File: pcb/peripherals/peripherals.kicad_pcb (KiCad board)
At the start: 2 copper layers, 31 parts, among them J1 JST XH, J10 JST XH, J11 JST XH, J2 JST XH, J3 Pin header, J4 Pin header, J5 JST XH, J6 JST XH, J7 JST XH, J8 JST XH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

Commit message: Route more tracks.
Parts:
- D1, D2: footprint Diode_THT:D_A-405_P10.16mm_Horizontal -> Diode_THT:D_A-405_P5.08mm_Vertical_KathodeUp
- moved J2 153.5 mm to (5.71, 57.1), turned to 90 degrees
- moved J8 151.5 mm to (26.0, 96.5), turned to 270 degrees
- moved J5 144.9 mm to (37.5, 96.5), turned to 270 degrees
- moved J1 115.0 mm to (14.0, 57.1), turned to 90 degrees
- moved REF** 110.5 mm to (128.3, 99.1)
- moved REF** 90.8 mm to (5.71, 101.6)
- moved J7 76.8 mm to (48.3, 96.5), turned to 270 degrees
- moved R1 69.5 mm to (44.5, 88.9)
- moved R3 69.3 mm to (44.5, 81.9)
- moved U2 68.9 mm to (97.8, 52.7), turned to 180 degrees
- moved REF** 64.1 mm to (127.0, 35.6)
- moved R5 63.5 mm to (50.2, 75.6)
- moved J11 57.8 mm to (125.7, 45.1), turned to 270 degrees
- moved J9 57.5 mm to (125.7, 83.8), turned to 270 degrees
- moved J6 52.8 mm to (15.2, 96.5), turned to 270 degrees
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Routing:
- net GND: track 0.00 -> 244.6 mm, vias 0 -> 2
- net +5V: track 0.00 -> 92.4 mm
- net SDA: track 0.00 -> 67.3 mm, vias 0 -> 2
- net +5VP: track 0.00 -> 59.4 mm, vias 0 -> 2
- net SCL: track 0.00 -> 57.2 mm
- net Net-(A1-Pad19): track 0.00 -> 51.6 mm, vias 0 -> 2
- net Net-(J3-Pad2): track 0.00 -> 40.8 mm, vias 0 -> 2
- net Net-(J4-Pad2): track 0.00 -> 36.2 mm, vias 0 -> 2
- net Net-(J1-Pad2): track 0.00 -> 8.26 mm

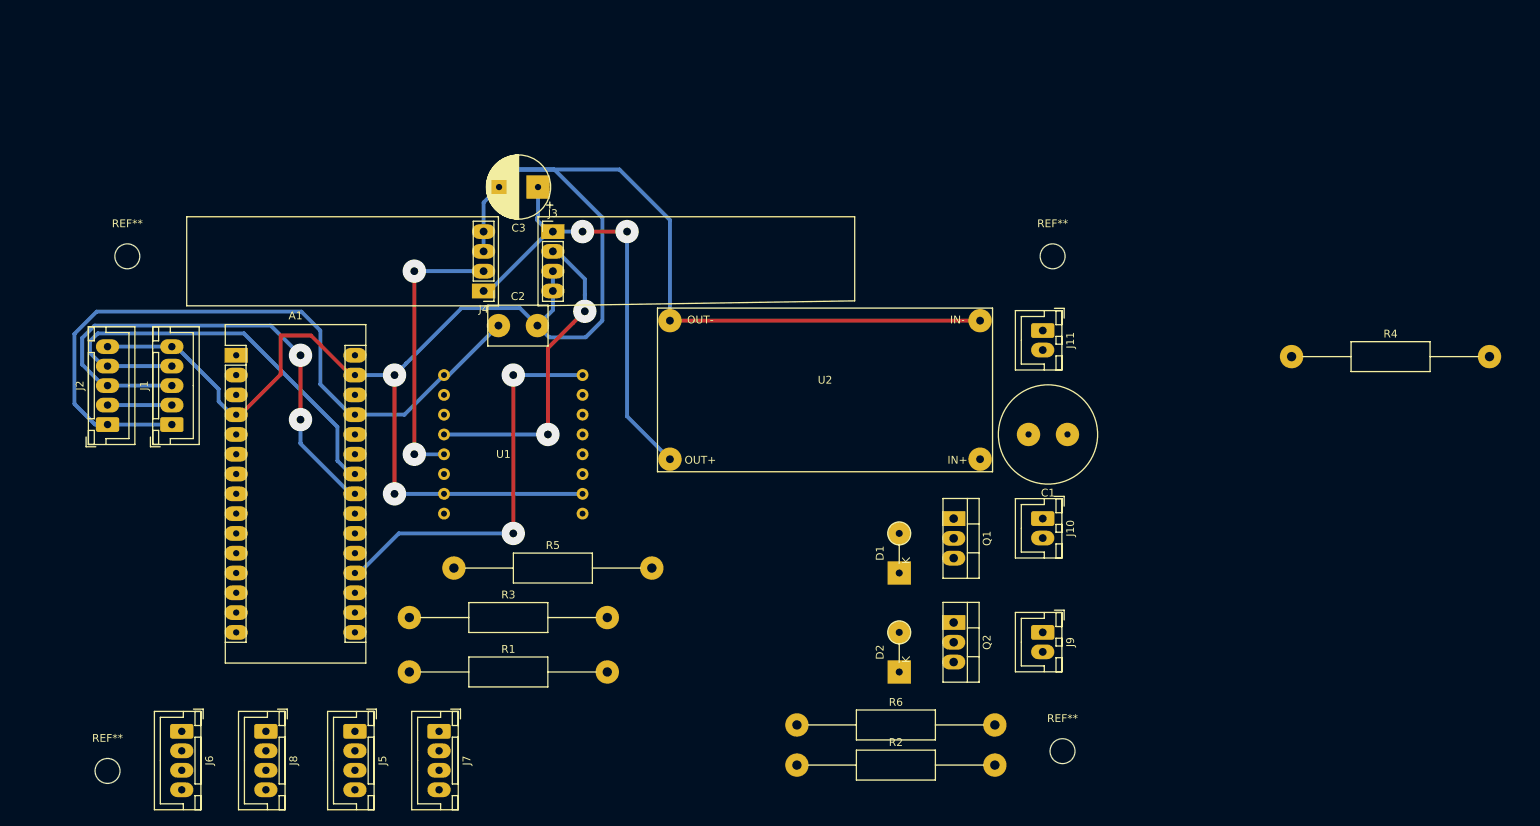
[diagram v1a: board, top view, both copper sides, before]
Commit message: Complete routing.
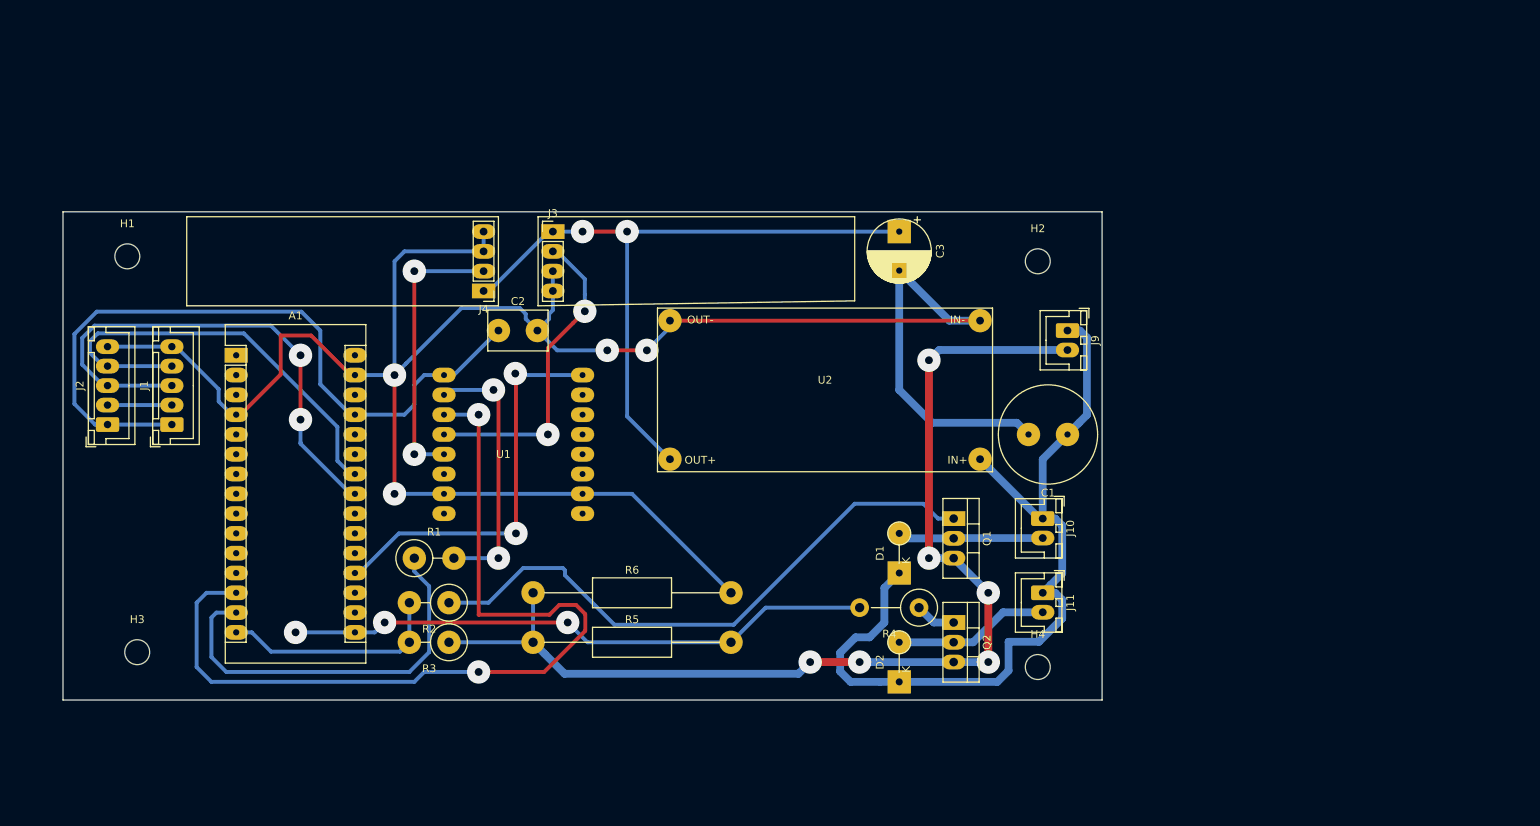
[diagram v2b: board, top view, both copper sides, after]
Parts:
- removed J5, J6, J7, J8: JST XH, Connector_JST:JST_XH_B04B-XH-A_1x04_P2.50mm_Vertical
- removed REF** (x4): MountingHole_3.2mm_M3, MountingHole:MountingHole_3.2mm_M3
- added H1: MountingHole, MountingHole:MountingHole_3.2mm_M3, F.Cu at (8.26, 35.6)
- added H2: MountingHole, MountingHole:MountingHole_3.2mm_M3, F.Cu at (125.1, 36.2)
- added H3: MountingHole, MountingHole:MountingHole_3.2mm_M3, F.Cu at (9.53, 86.4)
- added H4: MountingHole, MountingHole:MountingHole_3.2mm_M3, F.Cu at (125.1, 88.3)
- R1, R2, R3: footprint Resistor_THT:R_Axial_DIN0411_L9.9mm_D3.6mm_P25.40mm_Horizontal -> Resistor_THT:R_Axial_DIN0414_L11.9mm_D4.5mm_P5.08mm_Vertical
- R4: footprint Resistor_THT:R_Axial_DIN0411_L9.9mm_D3.6mm_P25.40mm_Horizontal -> Resistor_THT:R_Axial_DIN0414_L11.9mm_D4.5mm_P7.62mm_Vertical
- moved R4 57.7 mm to (109.9, 80.6), turned to 180 degrees
- moved R2 49.3 mm to (49.5, 80.0), turned to 180 degrees
- moved C3 46.7 mm to (107.3, 32.4), turned to 270 degrees
- moved J9 38.9 mm to (128.9, 45.1)
- moved R6 37.9 mm to (60.3, 78.7)
- moved J11 33.7 mm to (125.7, 78.7)
- moved R1 14.6 mm to (45.1, 74.3)
- moved R5 13.9 mm to (60.3, 85.1)
- moved R3 5.99 mm to (49.5, 85.1), turned to 180 degrees
- moved D2 1.27 mm to (107.3, 90.2)
- moved C2 0.63 mm to (55.9, 45.1)
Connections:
- A1 pad 10: IO6 -> Net-(A1-Pad10)
- A1 pad 11: IO7 -> Net-(A1-Pad11)
- A1 pad 12: IO8 -> Net-(A1-Pad12)
- A1 pad 5: IO1 -> Net-(A1-Pad5)
- A1 pad 6: IO2 -> Net-(A1-Pad6)
- A1 pad 7: IO3 -> Net-(A1-Pad7)
- A1 pad 8: IO4 -> Net-(A1-Pad8)
- A1 pad 9: IO5 -> Net-(A1-Pad9)
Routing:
- net GNDPWR: track 0.00 -> 139.9 mm, vias 0 -> 6
- net Net-(A1-Pad13): track 0.00 -> 114.2 mm, vias 0 -> 2
- net +24V: track 0.00 -> 108.9 mm
- net Net-(Q1-Pad1): track 0.00 -> 77.2 mm
- net PWM2: track 0.00 -> 75.8 mm, vias 0 -> 3
- net Net-(A1-Pad14): track 0.00 -> 51.2 mm
- net GND: track 244.6 -> 282.5 mm, vias 2 -> 4
- net Net-(R1-Pad2): track 0.00 -> 34.2 mm, vias 0 -> 2
- net PWM1: track 0.00 -> 28.8 mm
- net +5VP: track 59.4 -> 88.0 mm
- net Net-(D2-Pad2): track 0.00 -> 20.0 mm
- net Net-(D1-Pad2): track 0.00 -> 18.7 mm
- net Net-(Q2-Pad1): track 0.00 -> 5.23 mm
- net +5V: track 92.4 -> 94.3 mm
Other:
- board outline added: 133.3 x 62.7 mm

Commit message: Update.
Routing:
- net PWM2: track 75.8 -> 68.2 mm, vias 3 -> 2
- net +5VP: vias 2 -> 0
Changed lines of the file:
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@@
     (thickness 1.6)
     (drawings 12)
-    (tracks 250)
+    (tracks 246)
     (zones 0)
     (modules 27)
@@
   )
   (setup
-    (last_trace_width 0.5)
+    (last_trace_width 1)
     (user_trace_width 0.5)
     (trace_clearance 0.5)
@@
       (effects (font (size 1 1) (thickness 0.15)))
     )
-    (pad 1 thru_hole circle (at 0 0 180) (size 2.4 2.4) (drill 1.2) (layers *.Cu *.Mask)
+    (pad 1 thru_hole circle (at 0 0 180) (size 3 3) (drill 1.2) (layers *.Cu *.Mask)
       (net 31 "Net-(Q2-Pad1)"))
-    (pad 2 thru_hole oval (at 7.62 0 180) (size 2.4 2.4) (drill 1.2) (layers *.Cu *.Mask)
+    (pad 2 thru_hole oval (at 7.62 0 180) (size 3 3) (drill 1.2) (layers *.Cu *.Mask)
       (net 21 PWM2))
     (model ${KISYS3DMOD}/Resistor_THT.3dshapes/R_Axial_DIN0414_L11.9mm_D4.5mm_P7.62mm_Vertical.wrl
@@
   (segment (start 26.694999 86.289999) (end 24.225 83.82) (width 0.5) (layer B.Cu) (net 20))
   (segment (start 44.45 85.09) (end 43.250001 86.289999) (width 0.5) (layer B.Cu) (net 20))
-  (via (at 29.845 83.82) (size 3) (drill 1) (layers F.Cu B.Cu) (net 21))
-  (segment (start 37.465 83.82) (end 29.845 83.82) (width 0.5) (layer B.Cu) (net 21))
   (segment (start 90.17 80.645) (end 85.725 85.09) (width 0.5) (layer B.Cu) (net 21))
   (via (at 41.275 82.55) (size 3) (drill 1) (layers F.Cu B.Cu) (net 21))
@@
   (segment (start 54.695 40.005) (end 62.315 32.385) (width 0.5) (layer B.Cu) (net 26))
   (segment (start 53.975 40.005) (end 54.695 40.005) (width 0.5) (layer B.Cu) (net 26))
-  (via (at 66.675 32.385) (size 3) (drill 1) (layers F.Cu B.Cu) (net 26))
   (segment (start 62.865 32.385) (end 66.675 32.385) (width 0.5) (layer B.Cu) (net 26))
-  (via (at 72.39 32.385) (size 3) (drill 1) (layers F.Cu B.Cu) (net 26))
-  (segment (start 66.675 32.385) (end 72.39 32.385) (width 0.5) (layer F.Cu) (net 26))
   (segment (start 72.39 56.095) (end 77.89 61.595) (width 0.5) (layer B.Cu) (net 26))
   (segment (start 72.39 32.385) (end 72.39 56.095) (width 0.5) (layer B.Cu) (net 26))
   (segment (start 107.315 32.385) (end 72.39 32.385) (width 0.5) (layer B.Cu) (net 26))
+  (segment (start 66.675 32.385) (end 72.39 32.385) (width 0.5) (layer B.Cu) (net 26))
   (via (at 62.23 58.42) (size 3) (drill 1) (layers F.Cu B.Cu) (net 27))
   (segment (start 48.895 58.42) (end 62.23 58.42) (width 0.5) (layer B.Cu) (net 27))

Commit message: SMD version.
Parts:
- removed J10, J11: JST XH, Connector_JST:JST_XH_B02B-XH-A_1x02_P2.50mm_Vertical
- removed J4: Pin header, Connector_PinHeader_2.54mm:PinHeader_1x04_P2.54mm_Vertical
- removed U2: buck-converter, Peripherals:buck-converter
- added C4: 1u, Capacitor_SMD:C_0805_2012Metric, F.Cu at (25.4, 64.1)
- added C5: 1u, Capacitor_SMD:C_0805_2012Metric, F.Cu at (34.9, 64.1)
- added C6: 1u, Capacitor_SMD:C_0805_2012Metric, F.Cu at (64.8, 76.2)
- added C7: 1u, Capacitor_SMD:C_0805_2012Metric, F.Cu at (74.7, 76.2)
- added C9: 1u, Capacitor_SMD:C_0805_2012Metric, F.Cu at (62.9, 48.3)
- added D3: SS34, Diode_SMD:D_SMB, F.Cu at (69.8, 81.9)
- added D4: SS34, Diode_SMD:D_SMB, F.Cu at (79.4, 81.9)
- added J5: JST XH, Connector_JST:JST_XH_B02B-XH-A_1x02_P2.50mm_Vertical, F.Cu at (26.0, 87.6)
- added J6: JST XH, Connector_JST:JST_XH_B02B-XH-A_1x02_P2.50mm_Vertical, F.Cu at (35.6, 87.6)
- added J7: JST XH, Connector_JST:JST_XH_B02B-XH-A_1x02_P2.50mm_Vertical, F.Cu at (68.6, 87.6)
- added J8: JST XH, Connector_JST:JST_XH_B02B-XH-A_1x02_P2.50mm_Vertical, F.Cu at (78.1, 87.6)
- added Q3: FDD8447L, Package_TO_SOT_SMD:TO-252-2, F.Cu at (69.8, 73.7)
- added Q4: FDD8447L, Package_TO_SOT_SMD:TO-252-2, F.Cu at (79.4, 73.7)
- added R10: 47k, Resistor_SMD:R_0603_1608Metric, F.Cu at (77.5, 67.3)
- added R7: 1k, Resistor_SMD:R_0603_1608Metric, F.Cu at (71.8, 67.3)
- added R8: 47k, Resistor_SMD:R_0603_1608Metric, F.Cu at (67.9, 67.3)
- added R9: 1k, Resistor_SMD:R_0603_1608Metric, F.Cu at (81.3, 67.3)
- C1: footprint Capacitor_THT:C_Radial_D12.5mm_H20.0mm_P5.00mm -> Capacitor_SMD:CP_Elec_10x10
- C2: value 100n -> 1u; footprint Capacitor_THT:C_Disc_D7.5mm_W5.0mm_P5.00mm -> Capacitor_SMD:C_0603_1608Metric
- C3: footprint Capacitor_THT:CP_Radial_D8.0mm_P5.00mm -> Capacitor_SMD:CP_Elec_10x10
- D1, D2: value 1N4001 -> SS34; footprint Diode_THT:D_A-405_P5.08mm_Vertical_KathodeUp -> Diode_SMD:D_SMB
- J3: value Pin header -> Conn_01x03; footprint Connector_PinHeader_2.54mm:PinHeader_1x04_P2.54mm_Vertical -> Connector_JST:JST_XH_B03B-XH-A_1x03_P2.50mm_Vertical
- Q1, Q2: value IRFZ44N -> FDD8447L; footprint Package_TO_SOT_THT:TO-220-3_Vertical -> Package_TO_SOT_SMD:TO-252-2
- R1, R2, R3: footprint Resistor_THT:R_Axial_DIN0414_L11.9mm_D4.5mm_P5.08mm_Vertical -> Resistor_SMD:R_0603_1608Metric
- R4: footprint Resistor_THT:R_Axial_DIN0414_L11.9mm_D4.5mm_P7.62mm_Vertical -> Resistor_SMD:R_0603_1608Metric
- R5, R6: footprint Resistor_THT:R_Axial_DIN0411_L9.9mm_D3.6mm_P25.40mm_Horizontal -> Resistor_SMD:R_0603_1608Metric
- moved H4 119.6 mm to (19.7, 31.8)
- moved H2 117.3 mm to (19.7, 87.6)
- moved J9 108.8 mm to (20.3, 51.4)
- moved C1 99.2 mm to (29.8, 52.7), turned to 0 degrees
- moved H3 96.3 mm to (88.9, 31.8)
- moved H1 96.0 mm to (88.9, 87.6)
- moved Q1 87.1 mm to (27.3, 73.7)
- moved D1 80.2 mm to (27.3, 81.9), turned to 0 degrees
- moved Q2 78.0 mm to (36.8, 73.7)
- moved R4 72.4 mm to (38.7, 67.3)
- moved D2 71.0 mm to (36.8, 81.9), turned to 0 degrees
- moved C3 61.0 mm to (46.4, 33.7), turned to 0 degrees
- moved R1 34.4 mm to (66.0, 47.0)
- moved R6 34.4 mm to (39.4, 51.4)
- moved R5 31.0 mm to (34.9, 67.3)
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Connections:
- A1 pad 12: Net-(A1-Pad12) -> PWM4
- A1 pad 15: PWM1 -> Net-(A1-Pad15)
- A1 pad 16: PWM2 -> Net-(A1-Pad16)
- A1 pad 21: Net-(A1-Pad21) -> DFTX
- A1 pad 22: Net-(A1-Pad22) -> DFRX
- A1 pad 6: Net-(A1-Pad6) -> PWM1
- A1 pad 8: Net-(A1-Pad8) -> PWM2
- A1 pad 9: Net-(A1-Pad9) -> PWM3
- C1 pad 2: GND -> GNDPWR
- C3 pad 1: +5VP -> +5V
- J3 pad 1: +5VP -> Net-(J3-Pad1)
- J3 pad 2: Net-(J3-Pad2) -> GND
- J3 pad 3: GND -> Net-(J3-Pad3)
- R1 pad 1: Net-(A1-Pad14) -> DFRX
- U1 pad 3: Net-(A1-Pad13) -> DFTX
- U1 pad 4: Net-(J3-Pad2) -> Net-(J3-Pad3)
- U1 pad 5: Net-(J4-Pad2) -> Net-(J3-Pad1)
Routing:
- net GND: track 282.5 -> 147.1 mm, vias 4 -> 0
- net Net-(A1-Pad13): track 114.2 -> 0.00 mm, vias 2 -> 0
- net +5VP: track 88.0 -> 0.00 mm
- net Net-(Q1-Pad1): track 77.2 -> 2.32 mm
- net PWM4: track 0.00 -> 59.5 mm, vias 0 -> 1
- net PWM2: track 68.2 -> 11.9 mm, vias 2 -> 0
- net GNDPWR: track 139.9 -> 195.9 mm, vias 6 -> 0
- net Net-(A1-Pad14): track 51.2 -> 0.00 mm
- net PWM3: track 0.00 -> 47.1 mm, vias 0 -> 1
- net +24V: track 108.9 -> 152.3 mm
- net Net-(J3-Pad2): track 40.8 -> 0.00 mm, vias 2 -> 0
- net Net-(J4-Pad2): track 36.2 -> 0.00 mm, vias 2 -> 0
- net Net-(R1-Pad2): track 34.2 -> 4.29 mm, vias 2 -> 0
- net DFTX: track 0.00 -> 21.2 mm
- net Net-(J3-Pad1): track 0.00 -> 20.6 mm
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- added copper zone on F.Cu, net GND
- added copper zone on F.Cu, net GNDPWR
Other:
- board size 133.3 x 62.7 mm -> 77 x 64.5 mm
- board text added: "+"
- board text added: "24V"
- board text added: "AUDIO"
- board text added: "I2C"

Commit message: Work on layout.
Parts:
- removed the C2 at (81.9, 40.0)
- removed C7: 1u, Capacitor_SMD:C_0805_2012Metric
- removed the J3 at (71.8, 35.6)
- removed R10: 47k, Resistor_SMD:R_0603_1608Metric
- removed R9: 1k, Resistor_SMD:R_0603_1608Metric
- removed the U1 at (78.7, 44.5)
- added C4: 1u, Capacitor_SMD:C_0805_2012Metric, F.Cu at (14.0, 63.2)
- added J10: Conn_01x04, Connector_JST:JST_XH_B04B-XH-A_1x04_P2.50mm_Vertical, F.Cu at (38.3, 62.6)
- added J4: Conn_01x08, Connector_JST:JST_XH_B08B-XH-A_1x08_P2.50mm_Vertical, F.Cu at (39.1, 69.2)
- added J9: Conn_01x08, Connector_JST:JST_XH_B08B-XH-A_1x08_P2.50mm_Vertical, F.Cu at (66.0, 71.5)
- added Q5: MMBT3904, Package_TO_SOT_SMD:SOT-23, F.Cu at (31.0, 82.3)
- added Q6: IRFR5505TRPBF, Package_TO_SOT_SMD:TO-252-3_TabPin2, F.Cu at (20.5, 69.3)
- added Q7: MMBT3904, Package_TO_SOT_SMD:SOT-23, F.Cu at (30.6, 70.7)
- added Q8: IRFR5505TRPBF, Package_TO_SOT_SMD:TO-252-3_TabPin2, F.Cu at (21.0, 81.2)
- Q1, Q3: value FDD8447L -> MMBT3904; footprint Package_TO_SOT_SMD:TO-252-2 -> Package_TO_SOT_SMD:SOT-23
- Q2, Q4: value FDD8447L -> IRFR5505TRPBF; footprint Package_TO_SOT_SMD:TO-252-2 -> Package_TO_SOT_SMD:TO-252-3_TabPin2
- R2, R4: value 1k -> 10K
- R3, R5: value 47k -> 1k
- R6: value 100R -> 10K
- R8: value 47k -> 10K
- moved J8 72.0 mm to (6.53, 79.9), turned to 270 degrees
- moved D4 66.8 mm to (12.5, 81.0), turned to 270 degrees
- moved J7 65.1 mm to (6.53, 68.0), turned to 270 degrees
- moved Q4 60.8 mm to (20.6, 58.3), turned to 180 degrees
- moved D3 59.1 mm to (12.1, 69.3), turned to 270 degrees
- moved C6 52.0 mm to (13.7, 86.2), turned to 180 degrees
- moved J1 50.2 mm to (76.0, 40.4), turned to 270 degrees
- moved J5 45.9 mm to (6.53, 46.1), turned to 270 degrees
- moved R8 42.9 mm to (27.9, 82.6), turned to 270 degrees
- moved J2 42.3 mm to (68.8, 37.6), turned to 270 degrees
- moved Q3 42.3 mm to (29.9, 59.7), turned to 0 degrees
- moved J6 42.1 mm to (6.53, 57.1), turned to 270 degrees
- moved R7 41.4 mm to (30.3, 66.7), turned to 0 degrees
- moved D1 36.9 mm to (13.5, 47.7), turned to 270 degrees
- moved R1 35.0 mm to (31.1, 45.1)
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- renumbered C3 to C2, C4 to C3, J9 to J3, A1 to U1
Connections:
- C1 pad 2: GNDPWR -> GND
- C3 pad 2: GNDPWR -> GND
- C5 pad 2: GNDPWR -> GND
- C6 pad 2: GNDPWR -> GND
- D1 pad 1: +24V -> Net-(D1-Pad1)
- D1 pad 2: Net-(D1-Pad2) -> GND
- D2 pad 1: +24V -> Net-(D2-Pad1)
- D2 pad 2: Net-(D2-Pad2) -> GND
- D3 pad 1: +24V -> Net-(D3-Pad1)
- D3 pad 2: Net-(D3-Pad2) -> GND
- D4 pad 1: +24V -> Net-(D4-Pad1)
- D4 pad 2: Net-(D4-Pad2) -> GND
- J3 pad 2: GNDPWR -> GND
- J5 pad 1: +24V -> Net-(D1-Pad1)
- J5 pad 2: Net-(D1-Pad2) -> GND
- J6 pad 1: +24V -> Net-(D2-Pad1)
- J6 pad 2: Net-(D2-Pad2) -> GND
- J7 pad 1: +24V -> Net-(D3-Pad1)
- J7 pad 2: Net-(D3-Pad2) -> GND
- J8 pad 1: +24V -> Net-(D4-Pad1)
- J8 pad 2: Net-(D4-Pad2) -> GND
- Q1 pad 2: Net-(D1-Pad2) -> Net-(Q1-Pad2)
- Q1 pad 3: GNDPWR -> GND
- Q2 pad 1: Net-(Q2-Pad1) -> Net-(Q1-Pad2)
- Q2 pad 2: Net-(D2-Pad2) -> +24V
- Q2 pad 3: GNDPWR -> Net-(D1-Pad1)
- Q3 pad 2: Net-(D3-Pad2) -> Net-(Q3-Pad2)
- Q3 pad 3: GNDPWR -> GND
- Q4 pad 1: Net-(Q4-Pad1) -> Net-(Q3-Pad2)
- Q4 pad 2: Net-(D4-Pad2) -> +24V
- Q4 pad 3: GNDPWR -> Net-(D2-Pad1)
- R1 pad 1: DFRX -> Net-(Q1-Pad1)
- R1 pad 2: Net-(R1-Pad2) -> PWM1
- R2 pad 1: Net-(Q1-Pad1) -> +24V
- R2 pad 2: PWM1 -> Net-(Q1-Pad2)
- R3 pad 1: GNDPWR -> Net-(Q3-Pad1)
- R3 pad 2: PWM1 -> PWM2
- R4 pad 1: Net-(Q2-Pad1) -> +24V
- R4 pad 2: PWM2 -> Net-(Q3-Pad2)
- R5 pad 1: GNDPWR -> Net-(Q5-Pad1)
- R5 pad 2: PWM2 -> PWM3
- R6 pad 1: GNDPWR -> +24V
- R6 pad 2: GND -> Net-(Q5-Pad2)
- R7 pad 1: Net-(Q3-Pad1) -> Net-(Q7-Pad1)
- R7 pad 2: PWM3 -> PWM4
- R8 pad 1: GNDPWR -> +24V
- R8 pad 2: PWM3 -> Net-(Q7-Pad2)
- U1 pad 10: Net-(A1-Pad10) -> D7
- U1 pad 11: Net-(A1-Pad11) -> D8
- U1 pad 13: Net-(A1-Pad13) -> D10
- U1 pad 14: Net-(A1-Pad14) -> D11
- U1 pad 15: Net-(A1-Pad15) -> D12
- U1 pad 16: Net-(A1-Pad16) -> D13
- U1 pad 19: Net-(A1-Pad19) -> A0
- U1 pad 20: Net-(A1-Pad20) -> A1
- U1 pad 21: DFTX -> A2
- U1 pad 22: DFRX -> A3
- U1 pad 25: Net-(A1-Pad25) -> A6
- U1 pad 26: Net-(A1-Pad26) -> A7
- U1 pad 5: Net-(A1-Pad5) -> MPRX
- U1 pad 7: Net-(A1-Pad7) -> MPTX
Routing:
- net GNDPWR: track 195.9 -> 0.00 mm
- net +24V: track 152.3 -> 0.00 mm
- net GND: track 147.1 -> 32.1 mm, vias 0 -> 2
- net +5V: track 96.9 -> 8.09 mm, vias 2 -> 0
- net PWM4: track 59.5 -> 0.00 mm, vias 1 -> 0
- net SDA: track 58.8 -> 0.00 mm, vias 1 -> 0
- net Net-(A1-Pad19): track 54.7 -> 0.00 mm
- net SCL: track 53.9 -> 0.00 mm, vias 1 -> 0
- net PWM3: track 47.1 -> 0.00 mm, vias 1 -> 0
- net PWM1: track 23.3 -> 0.00 mm, vias 1 -> 0
- net D13: track 0.00 -> 22.8 mm
- net DFTX: track 21.2 -> 0.00 mm
- net Net-(J3-Pad1): track 20.6 -> 0.00 mm
- net Net-(J3-Pad3): track 20.0 -> 0.00 mm
- net DFRX: track 18.8 -> 0.00 mm
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- removed copper zone on F.Cu, net GND
- removed copper zone on F.Cu, net GNDPWR
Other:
- board text removed: "24V"
- board text removed: "AUDIO"
